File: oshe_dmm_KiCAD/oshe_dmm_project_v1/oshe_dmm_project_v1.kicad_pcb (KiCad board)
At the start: 4 copper layers, 101.6 x 177.8 mm, 79 parts, among them J1 FTDI Basic, J10 Voltage Range 2, J11 Voltage Range 3, J12 Voltage Range 3, J13 Current, J14 Resistance, J15 Resistance, J2 Voltage, J3 GND, J4 Current, J5 USB_C_Receptacle_PowerOnly_6P, J6 ON/OFF, J7 Voltage Range 1, J8 Voltage Range 1, J9 Voltage Range 2, SW1 PTS526 SK15 SMTR2 LFS, U1 ATmega328P-A, U2 INA219BxD, U3 BQ24075RGT, U4 LM317_SOT-223, U5 ADS1115IDGS, Y1 16MHz

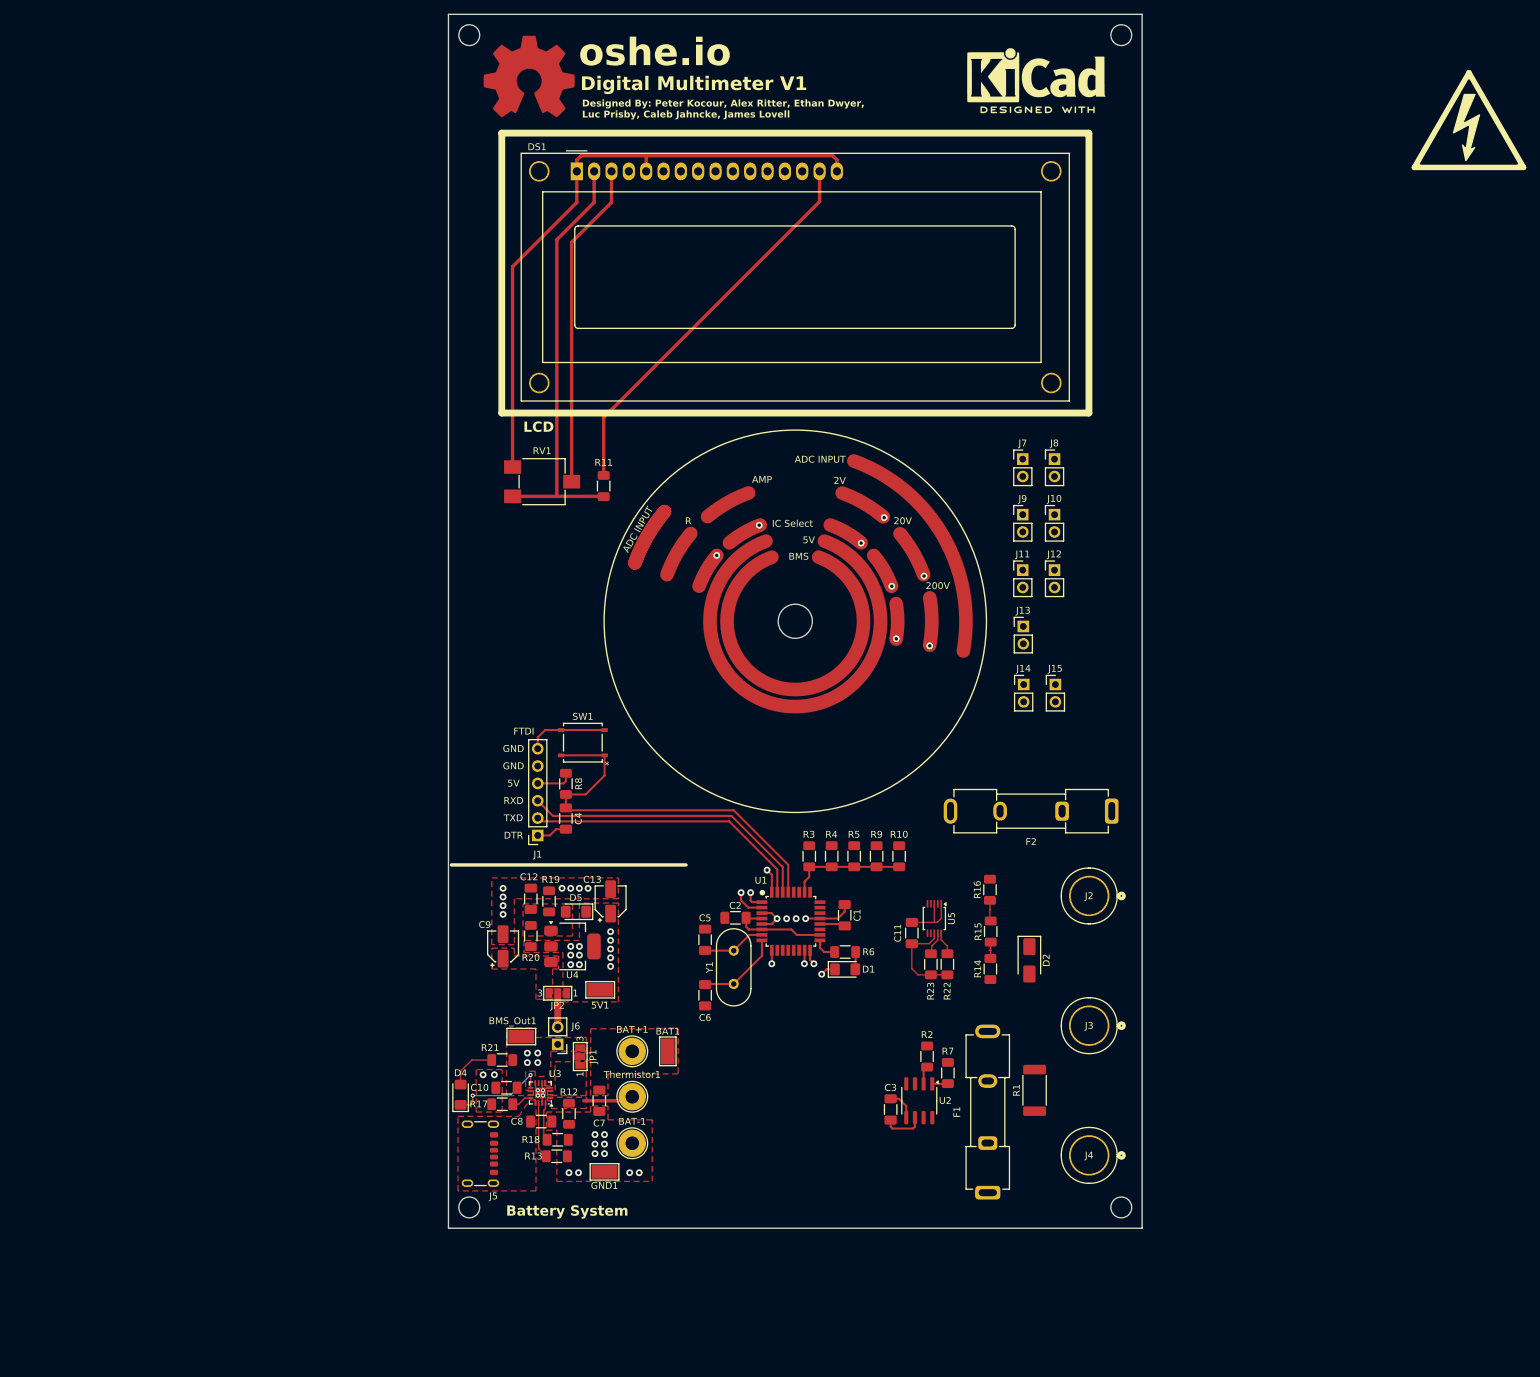
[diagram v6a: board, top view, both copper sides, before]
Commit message: Trying to fit everything on the board
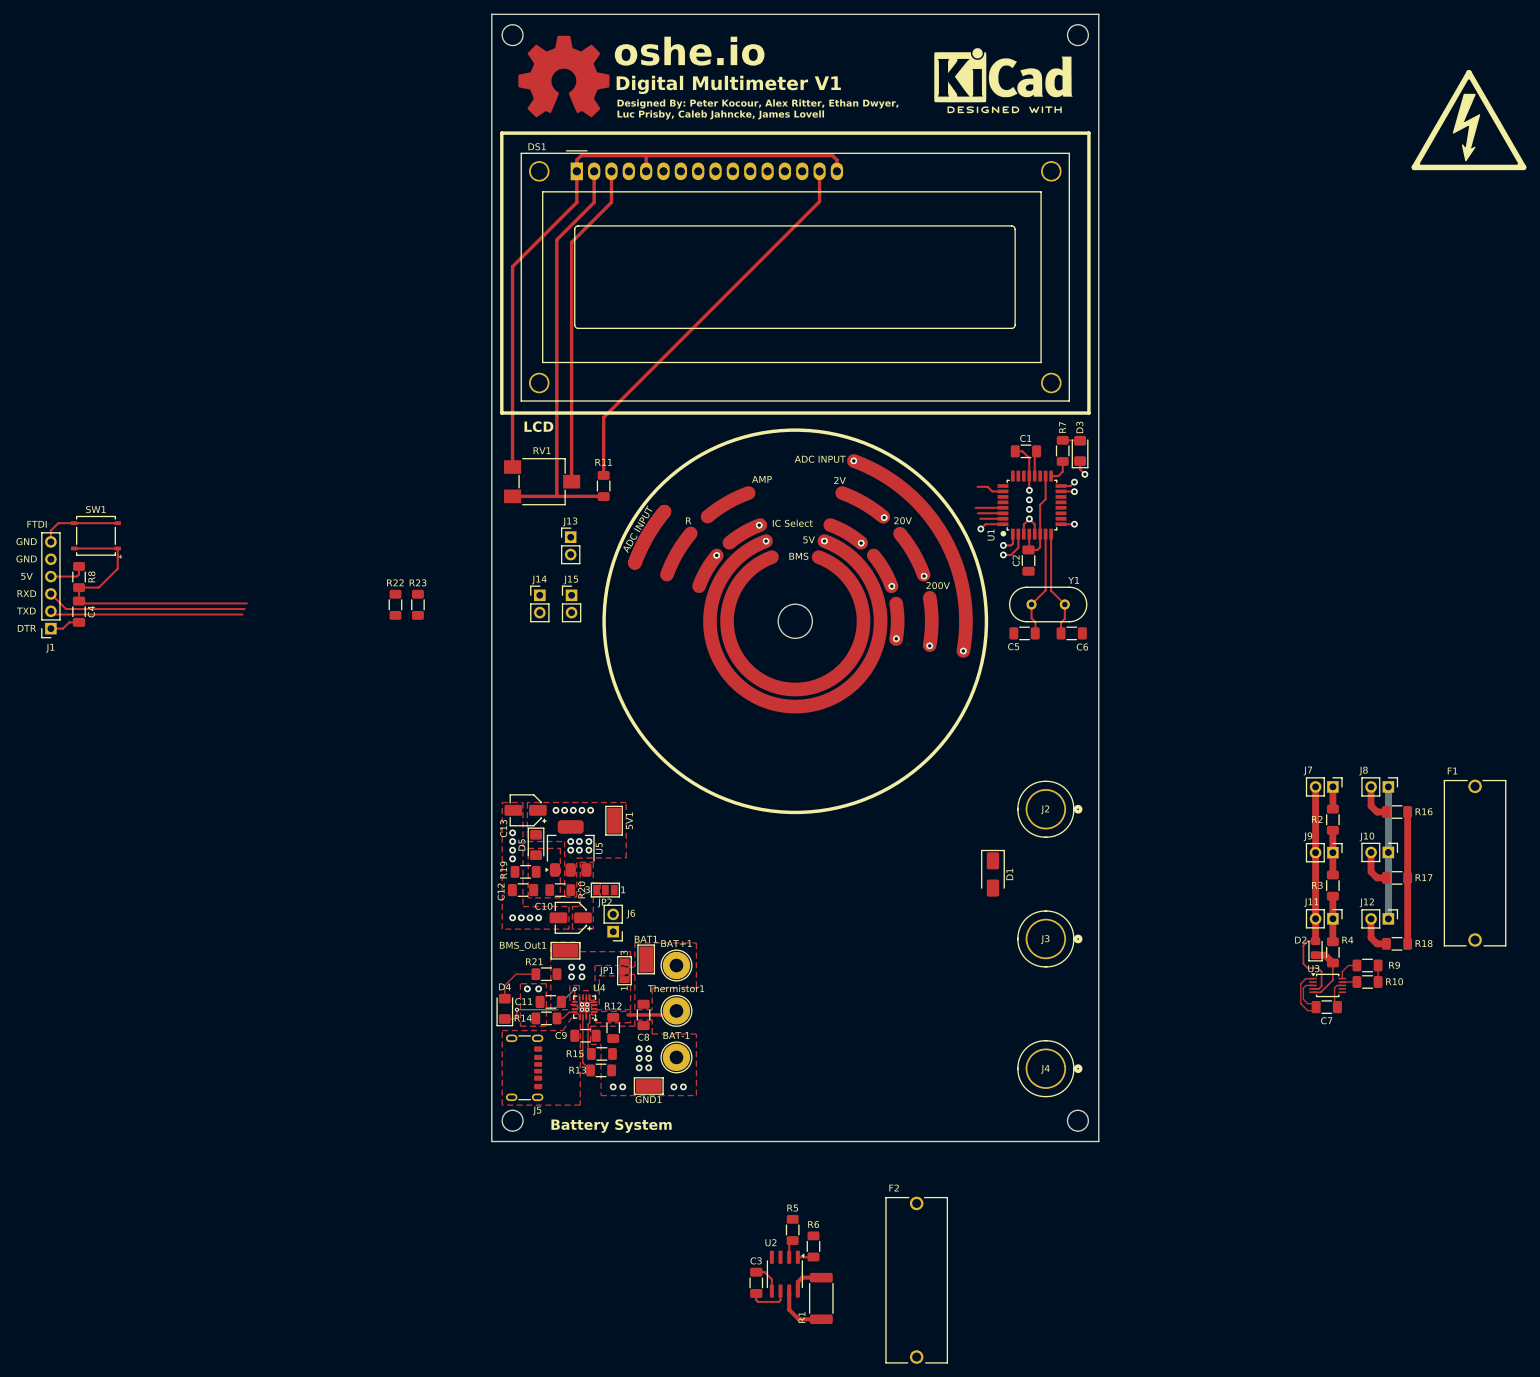
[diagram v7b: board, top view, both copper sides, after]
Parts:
- added D1: SMAJ200CA, Diode_SMD:D_SMA, F.Cu at (193.4, 189.2)
- D2: value SMAJ200CA -> D_TVS; footprint Diode_SMD:D_SMA -> Diode_SMD:D_0805_2012Metric_Pad1.15x1.40mm_HandSolder
- F1: value 5A -> 500mA; footprint Fuse:Fuseholder_Clip-5x20mm_Keystone_3512P_Inline_P23.62x7.27mm_D1.02x2.41x1.02x1.57mm_Horizontal -> DMM_Footprint_Library:FUSE_4628
- F2: value 500mA -> 5A; footprint Fuse:Fuseholder_Clip-5x20mm_Keystone_3512P_Inline_P23.62x7.27mm_D1.02x2.41x1.02x1.57mm_Horizontal -> DMM_Footprint_Library:FUSE_4628
- moved R16 86.3 mm to (252.6, 180.0), turned to 180 degrees
- moved F1 86.2 mm to (264.1, 187.5)
- moved D3 83.4 mm to (206.2, 127.1), turned to 90 degrees
- moved R17 82.9 mm to (252.6, 189.7), turned to 180 degrees
- moved R18 80.5 mm to (252.6, 199.3), turned to 180 degrees
- moved R7 80.0 mm to (203.7, 127.1), turned to -90 degrees
- moved R22 79.5 mm to (105.9, 149.7)
- moved R23 79.5 mm to (109.2, 149.7)
- moved R8 77.5 mm to (59.6, 145.6)
- moved C4 77.5 mm to (59.6, 150.7)
- moved J1 77.5 mm to (55.5, 153.2)
- moved SW1 77.5 mm to (62.1, 139.6)
- moved C6 75.4 mm to (205.0, 153.9), turned to 180 degrees
- moved F2 74.4 mm to (182.3, 248.6), turned to 90 degrees
- moved Y1 73.8 mm to (204.0, 149.6), turned to 180 degrees
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- renumbered C9 to C10, C10 to C11, C11 to C7, C7 to C8, C8 to C9, D1 to D3, R23 to R10, R17 to R14, R18 to R15, R3 to R16, R4 to R17, R5 to R18, R14 to R2, R9 to R22, R10 to R23, R15 to R3, R16 to R4, R2 to R5, R7 to R6, R6 to R7, R22 to R9, U5 to U3, U3 to U4, U4 to U5
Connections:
- D2 pad 1: 2V_Rang -> Input_Negative
- D2 pad 2: Input_Negative -> V_ADC_Input
- F1 pad 1: Current_Input -> Voltage_Input
- F1 pad 2: Net-(U2-IN+) -> 2V_Rang
- F2 pad 1: Voltage_Input -> Current_Input
- F2 pad 2: 2V_Rang -> Net-(U2-IN+)
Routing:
- net V_ADC_Input: track 0.00 -> 34.0 mm, vias 0 -> 2
- net Input_Negative: track 0.00 -> 17.2 mm
- net +5V: track 101.7 -> 114.1 mm, vias 11 -> 13
- net Net-(U1-~{RESET}/PC6): track 58.1 -> 46.9 mm
- net RXD: track 43.6 -> 33.0 mm
- net TXD: track 41.5 -> 31.6 mm
- net Net-(U1-XTAL1/PB6): track 9.29 -> 15.7 mm
- net A3: track 17.3 -> 23.3 mm
- net Net-(J10-Pin_2): track 0.00 -> 5.47 mm, vias 0 -> 1
- net Net-(J12-Pin_2): track 0.00 -> 5.39 mm, vias 0 -> 1
- net Net-(J8-Pin_2): track 0.00 -> 5.29 mm, vias 0 -> 1
- net Net-(U2-IN+): track 0.00 -> 5.02 mm
- net Net-(J6-Pin_2): track 4.95 -> 0.00 mm
- net GND: track 141.0 -> 145.1 mm
- net 20V_Rang: track 2.62 -> 6.55 mm, vias 0 -> 1
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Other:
- board size 101.6 x 177.8 mm -> 88.9 x 165.1 mm

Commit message: PCB is almost done!
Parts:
- removed J14, J15: Resistance, Connector_PinHeader_2.54mm:PinHeader_1x02_P2.54mm_Vertical
- removed R23: 1k, Resistor_SMD:R_1206_3216Metric_Pad1.30x1.75mm_HandSolder
- moved J8 107.3 mm to (144.4, 184.2), turned to 0 degrees
- moved R16 104.3 mm to (148.4, 185.2), turned to -90 degrees
- moved J7 100.0 mm to (144.4, 191.4), turned to 0 degrees
- moved J10 97.4 mm to (154.0, 184.2), turned to 0 degrees
- moved D3 97.3 mm to (127.8, 184.7), turned to -90 degrees
- moved R17 94.7 mm to (158.0, 185.2), turned to -90 degrees
- moved R2 94.6 mm to (149.2, 191.4), turned to 0 degrees
- moved R7 93.2 mm to (130.3, 184.7), turned to 90 degrees
- moved J9 89.4 mm to (154.0, 191.4), turned to 0 degrees
- moved J12 88.4 mm to (163.7, 184.2), turned to 0 degrees
- moved R18 86.1 mm to (167.7, 185.2), turned to -90 degrees
- moved C1 85.8 mm to (134.6, 184.6), turned to 180 degrees
- moved R3 84.4 mm to (158.8, 191.4), turned to 0 degrees
- moved C6 82.4 mm to (123.4, 165.5), turned to -90 degrees
- moved REF** 81.8 mm to (199.6, 130.2)
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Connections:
- DS1 pad 4: MOSI/D11 -> MISO/D12
- DS1 pad 6: MISO/D12 -> MOSI/D11
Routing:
- net V_ADC_Input: track 34.0 -> 84.4 mm
- net 2V_Rang: track 3.26 -> 53.7 mm
- net Input_Negative: track 17.2 -> 49.8 mm
- net A3: track 23.3 -> 49.1 mm
- net +5V: track 114.1 -> 88.8 mm, vias 13 -> 15
- net Net-(U2-IN+): track 5.02 -> 29.5 mm
- net Net-(U1-~{RESET}/PC6): track 46.9 -> 58.1 mm
- net Voltage_Input: track 0.00 -> 9.96 mm
- net RXD: track 33.0 -> 42.3 mm
- net Net-(J6-Pin_2): track 0.00 -> 7.41 mm
- net TXD: track 31.6 -> 38.9 mm
- net Net-(J13-Pin_2): track 0.00 -> 4.03 mm
- net Net-(U1-XTAL2/PB7): track 15.6 -> 11.7 mm
- net Net-(U2-A0): track 2.84 -> 0.00 mm
- net SDA: track 2.15 -> 4.69 mm
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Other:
- board text removed: "Battery System"
